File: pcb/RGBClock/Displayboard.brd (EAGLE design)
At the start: 70 x 58.5 mm, 66 parts, among them IC1 MCP23017SO, U1 LP3878MR-ADJ, U2 P82B96DR, U3 P82B96DR, U4 PCA9685PW, U5 TPS71533DCKR, U6 ZXLD1362ET5TA, U7 74HCT1G14GW, U8 74HCT1G86GW, X1 43045-0400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

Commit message: Just before freerouter
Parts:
- moved R3 14.5 mm to (26.0, 27.9), turned to 0 degrees
- moved R4 13.0 mm to (26.0, 24.1), turned to 0 degrees
- moved C7 7.17 mm to (40.6, 25.4)
- moved C5 6.91 mm to (32.4, 25.4)
- moved U5 6.72 mm to (36.2, 25.4)
- moved D4 4.96 mm to (12.7, 5.71), turned to 180 degrees
- moved X6 4.02 mm to (66.0, 49.5)
- moved R13 3.92 mm to (22.9, 15.9)
- moved R14 3.92 mm to (19.1, 15.9)
- moved C12 3.52 mm to (19.1, 3.81)
- moved C10 3.49 mm to (19.1, 6.99)
- moved C8 3.47 mm to (19.1, 13.3)
- moved C9 3.45 mm to (19.1, 10.2)
- moved R12 3.01 mm to (19.1, 1.91)
- moved C11 2.74 mm to (24.8, 7.62)
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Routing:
- net +5V: track 175.3 -> 0.00 mm
- net SDA: track 115.1 -> 0.00 mm, vias 6 -> 0
- net SCL: track 96.2 -> 0.00 mm, vias 8 -> 0
- net VCC: track 60.0 -> 0.00 mm
- net RS: track 44.0 -> 0.00 mm, vias 4 -> 0
- net +3V3: track 42.3 -> 0.00 mm, vias 2 -> 0
- net N$22: track 40.1 -> 0.00 mm, vias 4 -> 0
- net N$12: track 37.2 -> 0.00 mm, vias 2 -> 0
- net D2: track 34.6 -> 0.00 mm, vias 2 -> 0
- net N$2: track 32.5 -> 0.00 mm, vias 2 -> 0
- net RW: track 26.9 -> 0.00 mm, vias 3 -> 0
- net N$9: track 26.7 -> 0.00 mm, vias 3 -> 0
- net D0: track 25.0 -> 0.00 mm, vias 2 -> 0
- net N$49: track 22.4 -> 0.00 mm
- net N$3: track 21.3 -> 0.00 mm, vias 2 -> 0
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- removed copper zone on layer 1, net GND
- removed copper zone on layer 16, net GND

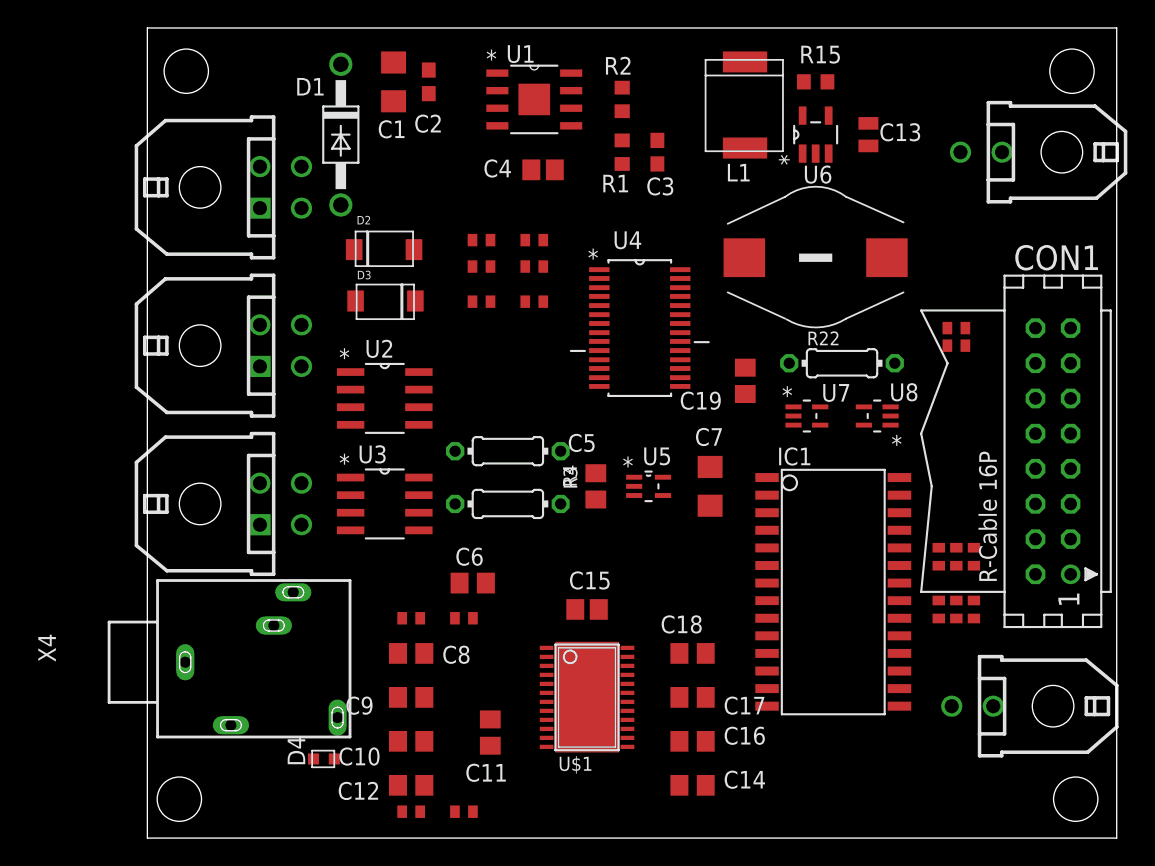
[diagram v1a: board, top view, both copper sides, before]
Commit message: Leddriver board complete
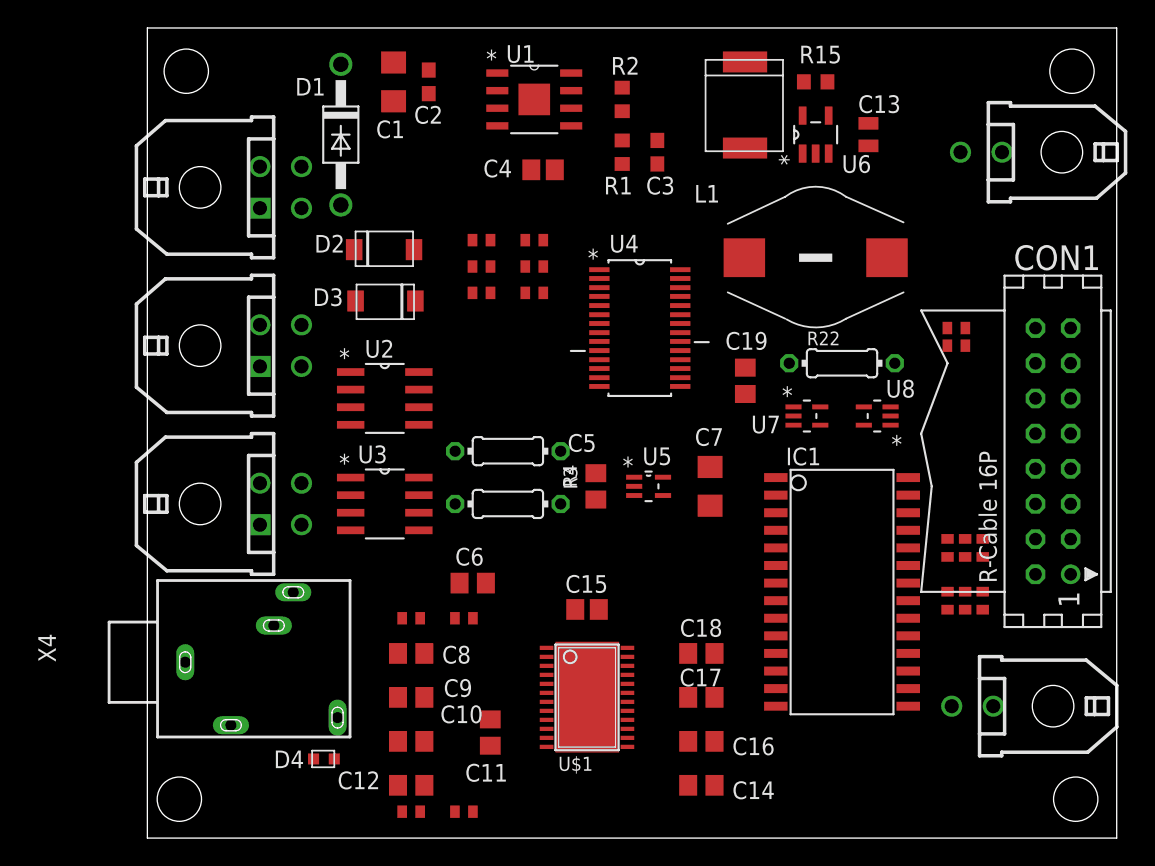
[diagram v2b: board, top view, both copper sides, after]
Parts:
- moved R16 0.90 mm to (60.3, 17.1)
- moved R17 0.90 mm to (60.3, 21.0)
- moved R18 0.90 mm to (59.1, 17.1)
- moved R19 0.90 mm to (59.1, 21.0)
- moved R20 0.90 mm to (57.8, 17.1)
- moved R21 0.90 mm to (57.8, 21.0)
- moved C14 0.64 mm to (40.0, 3.81)
- moved C16 0.64 mm to (40.0, 6.99)
- moved C17 0.64 mm to (40.0, 10.2)
- moved C18 0.64 mm to (40.0, 13.3)
- moved IC1 0.63 mm to (50.2, 18.4)
- moved R5 0.63 mm to (27.9, 39.4)
- moved R6 0.63 mm to (24.1, 39.4)

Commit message: Mainboard routable !
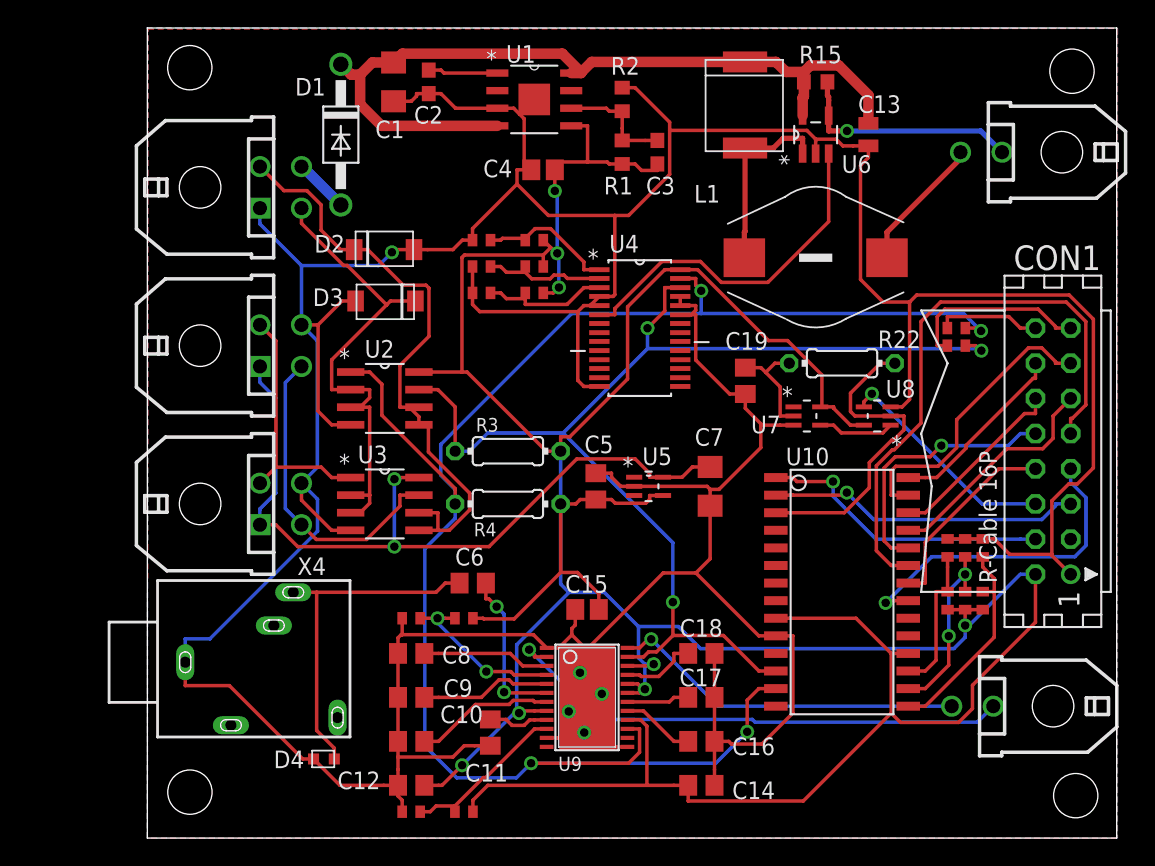
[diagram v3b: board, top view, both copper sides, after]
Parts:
- renumbered IC1 to U10, U$1 to U9
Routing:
- net GND: track 0.00 -> 375.3 mm, vias 0 -> 5
- net +5V: track 0.00 -> 272.3 mm, vias 0 -> 8
- net SDA: track 0.00 -> 126.1 mm, vias 0 -> 4
- net SCL: track 0.00 -> 85.1 mm, vias 0 -> 3
- net VCC: track 0.00 -> 60.0 mm
- net +3V3: track 0.00 -> 55.9 mm, vias 0 -> 2
- net N$22: track 0.00 -> 44.3 mm
- net D2: track 0.00 -> 42.4 mm
- net N$12: track 0.00 -> 37.7 mm, vias 0 -> 1
- net N$2: track 0.00 -> 35.3 mm
- net N$8: track 0.00 -> 25.8 mm
- net N$11: track 0.00 -> 25.7 mm, vias 0 -> 1
- net N$49: track 0.00 -> 24.8 mm
- net D0: track 0.00 -> 23.9 mm, vias 0 -> 1
- net N$3: track 0.00 -> 23.2 mm
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- added copper zone on layer 1, net GND
- added copper zone on layer 16, net GND
